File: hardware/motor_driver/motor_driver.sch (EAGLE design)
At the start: 88 parts

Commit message: Shit from Sunday work session
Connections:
- net DC_CAL: now also CURR-4.S; no longer CURR-2.S
- net DGND: now also M-1.S; no longer M-8.S
- net EN_GATE: now also M-2.S; no longer M-1.S
- net H1: now also M-3.S; no longer M-2.S
- net H2: now also M-5.S; no longer M-4.S
- net H3: now also M-7.S; no longer M-6.S
- net L1: now also M-4.S; no longer M-3.S
- net L2: now also M-6.S; no longer M-5.S
- net L3: now also M-8.S; no longer M-7.S
- net REF: now also CURR-3.S; no longer CURR-1.S
- net SO1: now also CURR-2.S; no longer CURR-3.S
- net SO2: now also CURR-1.S; no longer CURR-4.S
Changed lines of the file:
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@@
 <?xml version="1.0" encoding="utf-8"?>
 <!DOCTYPE eagle SYSTEM "eagle.dtd">
-<eagle version="7.3.0">
+<eagle version="7.2.0">
 <drawing>
 <settings>
@@
 </segment>
 <segment>
-<pinref part="M" gate="-2" pin="S"/>
-<wire x1="248.92" y1="45.72" x2="248.92" y2="48.26" width="0.1524" layer="91"/>
-<label x="248.92" y="48.26" size="1.016" layer="95" rot="R90" xref="yes"/>
+<pinref part="M" gate="-3" pin="S"/>
+<wire x1="246.38" y1="45.72" x2="246.38" y2="48.26" width="0.1524" layer="91"/>
+<label x="246.38" y="48.26" size="1.016" layer="95" rot="R90" xref="yes"/>
 </segment>
 </net>
@@
 </segment>
 <segment>
-<pinref part="M" gate="-3" pin="S"/>
-<wire x1="246.38" y1="45.72" x2="246.38" y2="48.26" width="0.1524" layer="91"/>
-<label x="246.38" y="48.26" size="1.016" layer="95" rot="R90" xref="yes"/>
+<pinref part="M" gate="-4" pin="S"/>
+<wire x1="243.84" y1="45.72" x2="243.84" y2="48.26" width="0.1524" layer="91"/>
+<label x="243.84" y="48.26" size="1.016" layer="95" rot="R90" xref="yes"/>
 </segment>
 </net>
@@
 </segment>
 <segment>
-<pinref part="M" gate="-4" pin="S"/>
-<wire x1="243.84" y1="45.72" x2="243.84" y2="48.26" width="0.1524" layer="91"/>
-<label x="243.84" y="48.26" size="1.016" layer="95" rot="R90" xref="yes"/>
+<pinref part="M" gate="-5" pin="S"/>
+<wire x1="241.3" y1="45.72" x2="241.3" y2="48.26" width="0.1524" layer="91"/>
+<label x="241.3" y="48.26" size="1.016" layer="95" rot="R90" xref="yes"/>
 </segment>
 </net>
@@
 </segment>
 <segment>
-<pinref part="M" gate="-5" pin="S"/>
-<wire x1="241.3" y1="45.72" x2="241.3" y2="48.26" width="0.1524" layer="91"/>
-<label x="241.3" y="48.26" size="1.016" layer="95" rot="R90" xref="yes"/>
+<pinref part="M" gate="-6" pin="S"/>
+<wire x1="238.76" y1="45.72" x2="238.76" y2="48.26" width="0.1524" layer="91"/>
+<label x="238.76" y="48.26" size="1.016" layer="95" rot="R90" xref="yes"/>
 </segment>
 </net>
@@
 </segment>
 <segment>
-<pinref part="M" gate="-6" pin="S"/>
-<wire x1="238.76" y1="45.72" x2="238.76" y2="48.26" width="0.1524" layer="91"/>
-<label x="238.76" y="48.26" size="1.016" layer="95" rot="R90" xref="yes"/>
+<pinref part="M" gate="-7" pin="S"/>
+<wire x1="236.22" y1="45.72" x2="236.22" y2="48.26" width="0.1524" layer="91"/>
+<label x="236.22" y="48.26" size="1.016" layer="95" rot="R90" xref="yes"/>
 </segment>
 </net>
@@
 </segment>
 <segment>
-<pinref part="M" gate="-7" pin="S"/>
-<wire x1="236.22" y1="45.72" x2="236.22" y2="48.26" width="0.1524" layer="91"/>
-<label x="236.22" y="48.26" size="1.016" layer="95" rot="R90" xref="yes"/>
+<pinref part="M" gate="-8" pin="S"/>
+<wire x1="233.68" y1="45.72" x2="233.68" y2="48.26" width="0.1524" layer="91"/>
+<label x="233.68" y="48.26" size="1.016" layer="95" rot="R90" xref="yes"/>
 </segment>
 </net>
@@
 </segment>
 <segment>
-<pinref part="M" gate="-1" pin="S"/>
-<wire x1="251.46" y1="45.72" x2="251.46" y2="48.26" width="0.1524" layer="91"/>
-<label x="251.46" y="48.26" size="1.016" layer="95" rot="R90" xref="yes"/>
+<pinref part="M" gate="-2" pin="S"/>
+<wire x1="248.92" y1="45.72" x2="248.92" y2="48.26" width="0.1524" layer="91"/>
+<label x="248.92" y="48.26" size="1.016" layer="95" rot="R90" xref="yes"/>
 </segment>
 </net>
@@
 </segment>
 <segment>
-<pinref part="CURR" gate="-2" pin="S"/>
-<wire x1="259.08" y1="-78.74" x2="259.08" y2="-76.2" width="0.1524" layer="91"/>
-<label x="259.08" y="-78.74" size="1.016" layer="95" rot="R270" xref="yes"/>
+<pinref part="CURR" gate="-4" pin="S"/>
+<wire x1="264.16" y1="-76.2" x2="264.16" y2="-78.74" width="0.1524" layer="91"/>
+<label x="264.16" y="-78.74" size="1.016" layer="95" rot="R270" xref="yes"/>
 </segment>
 </net>
@@
 </segment>
 <segment>
-<pinref part="CURR" gate="-1" pin="S"/>
-<wire x1="256.54" y1="-78.74" x2="256.54" y2="-76.2" width="0.1524" layer="91"/>
-<label x="256.54" y="-78.74" size="1.016" layer="95" rot="R270" xref="yes"/>
+<pinref part="CURR" gate="-3" pin="S"/>
+<wire x1="261.62" y1="-78.74" x2="261.62" y2="-76.2" width="0.1524" layer="91"/>
+<label x="261.62" y="-78.74" size="1.016" layer="95" rot="R270" xref="yes"/>
 </segment>
 </net>
@@
 </segment>
 <segment>
-<pinref part="CURR" gate="-4" pin="S"/>
-<wire x1="264.16" y1="-76.2" x2="264.16" y2="-78.74" width="0.1524" layer="91"/>
-<label x="264.16" y="-78.74" size="1.016" layer="95" rot="R270" xref="yes"/>
+<pinref part="CURR" gate="-1" pin="S"/>
+<wire x1="256.54" y1="-78.74" x2="256.54" y2="-76.2" width="0.1524" layer="91"/>
+<label x="256.54" y="-78.74" size="1.016" layer="95" rot="R270" xref="yes"/>
 </segment>
 </net>
@@
 </segment>
 <segment>
-<pinref part="CURR" gate="-3" pin="S"/>
-<wire x1="261.62" y1="-78.74" x2="261.62" y2="-76.2" width="0.1524" layer="91"/>
-<label x="261.62" y="-78.74" size="1.016" layer="95" rot="R270" xref="yes"/>
+<pinref part="CURR" gate="-2" pin="S"/>
+<wire x1="259.08" y1="-78.74" x2="259.08" y2="-76.2" width="0.1524" layer="91"/>
+<label x="259.08" y="-78.74" size="1.016" layer="95" rot="R270" xref="yes"/>
 </segment>
 </net>
@@
 </segment>
 <segment>
-<pinref part="M" gate="-8" pin="S"/>
-<wire x1="233.68" y1="45.72" x2="233.68" y2="48.26" width="0.1524" layer="91"/>
-<label x="233.68" y="48.26" size="1.016" layer="95" rot="R90" xref="yes"/>
-</segment>
-<segment>
 <pinref part="R16" gate="G$1" pin="1"/>
 <pinref part="SUPPLY6" gate="G$1" pin="DGND"/>
@@
 <pinref part="SUPPLY13" gate="G$1" pin="DGND"/>
 </segment>
-</net>
+<segment>
+<pinref part="M" gate="-1" pin="S"/>
+<wire x1="251.46" y1="45.72" x2="251.46" y2="48.26" width="0.1524" layer="91"/>
+<label x="251.46" y="48.26" size="1.016" layer="95" rot="R90" xref="yes"/>
+</segment>
+</net>

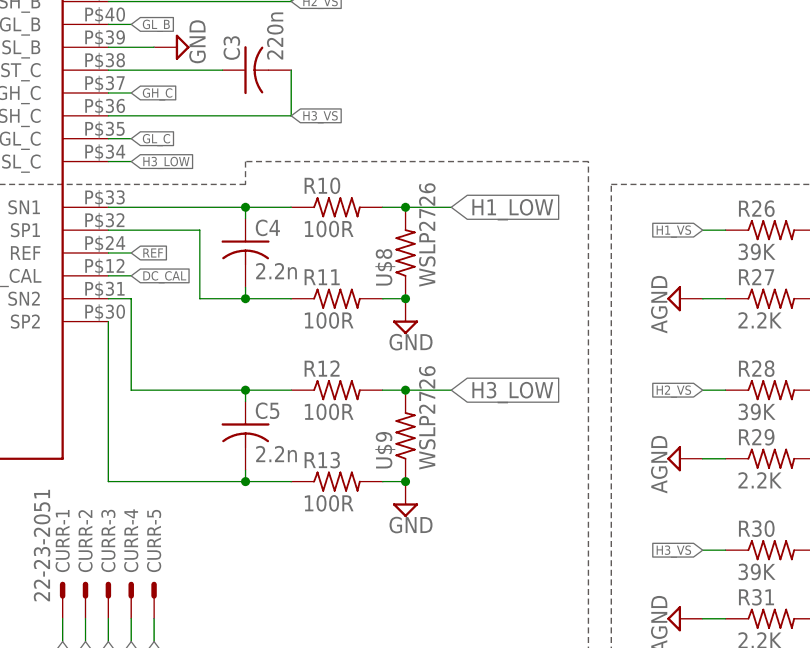
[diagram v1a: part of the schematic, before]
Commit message: Changed shunt resistor sch, needs confirmtion
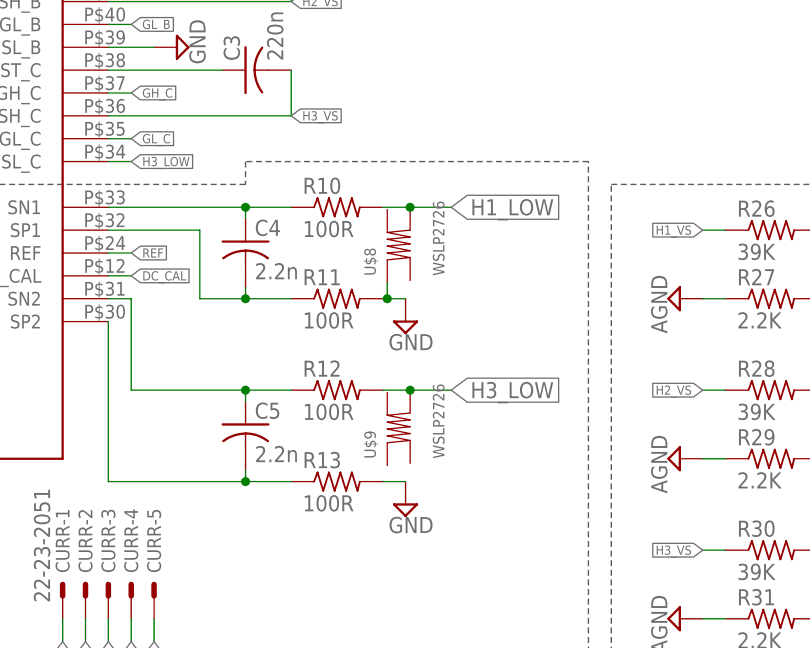
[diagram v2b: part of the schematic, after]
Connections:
- net GND: now also U$8.P$4; no longer U$8.1, U$9.1
- net H1_LOW: now also U$8.P$1; no longer U$8.2
- net H3_LOW: now also U$9.P$1; no longer U$9.2
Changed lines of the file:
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@@
 <part name="R12" library="adafruit" deviceset="R-US_" device="R0603" value="100R"/>
 <part name="R13" library="adafruit" deviceset="R-US_" device="R0603" value="100R"/>
-<part name="U$8" library="bldc_lib" deviceset="WSLP2726" device=""/>
-<part name="U$9" library="bldc_lib" deviceset="WSLP2726" device=""/>
 <part name="SUPPLY1" library="supply2" deviceset="GND" device=""/>
 <part name="SUPPLY2" library="supply2" deviceset="GND" device=""/>
@@
 <part name="SUPPLY27" library="supply2" deviceset="GND" device=""/>
 <part name="SUPPLY13" library="supply2" deviceset="DGND" device=""/>
+<part name="U$8" library="bldc_lib" deviceset="WSLP2726" device=""/>
+<part name="U$9" library="bldc_lib" deviceset="WSLP2726" device=""/>
 </parts>
 <sheets>
@@
 <instance part="R12" gate="G$1" x="287.02" y="-50.8"/>
 <instance part="R13" gate="G$1" x="287.02" y="-60.96"/>
-<instance part="U$8" gate="R$1" x="294.64" y="-35.56" rot="R90"/>
-<instance part="U$9" gate="R$1" x="294.64" y="-55.88" rot="R90"/>
 <instance part="SUPPLY1" gate="GND" x="294.64" y="-43.18"/>
 <instance part="SUPPLY2" gate="GND" x="294.64" y="-63.5"/>
@@
 <instance part="SUPPLY27" gate="GND" x="269.24" y="-12.7" rot="R90"/>
 <instance part="SUPPLY13" gate="G$1" x="200.66" y="-17.78" rot="R180"/>
+<instance part="U$8" gate="G$1" x="293.878" y="-35.56" rot="R90"/>
+<instance part="U$9" gate="G$1" x="293.878" y="-55.88" rot="R90"/>
 </instances>
 <busses>
@@
 <segment>
 <pinref part="R10" gate="G$1" pin="2"/>
-<pinref part="U$8" gate="R$1" pin="2"/>
-<wire x1="292.1" y1="-30.48" x2="294.64" y2="-30.48" width="0.1524" layer="91"/>
-<wire x1="294.64" y1="-30.48" x2="299.72" y2="-30.48" width="0.1524" layer="91"/>
-<junction x="294.64" y="-30.48"/>
+<wire x1="292.1" y1="-30.48" x2="295.148" y2="-30.48" width="0.1524" layer="91"/>
 <label x="299.72" y="-30.48" size="1.778" layer="95" xref="yes"/>
+<pinref part="U$8" gate="G$1" pin="P$1"/>
+<wire x1="295.148" y1="-30.48" x2="299.72" y2="-30.48" width="0.1524" layer="91"/>
+<junction x="295.148" y="-30.48"/>
 </segment>
 </net>
@@
 </segment>
 <segment>
-<pinref part="U$9" gate="R$1" pin="2"/>
 <pinref part="R12" gate="G$1" pin="2"/>
-<wire x1="294.64" y1="-50.8" x2="292.1" y2="-50.8" width="0.1524" layer="91"/>
-<wire x1="294.64" y1="-50.8" x2="299.72" y2="-50.8" width="0.1524" layer="91"/>
-<junction x="294.64" y="-50.8"/>
+<wire x1="292.1" y1="-50.8" x2="295.148" y2="-50.8" width="0.1524" layer="91"/>
 <label x="299.72" y="-50.8" size="1.778" layer="95" xref="yes"/>
+<pinref part="U$9" gate="G$1" pin="P$1"/>
+<wire x1="295.148" y1="-50.8" x2="299.72" y2="-50.8" width="0.1524" layer="91"/>
+<junction x="295.148" y="-50.8"/>
 </segment>
 </net>
@@
 <segment>
 <pinref part="R11" gate="G$1" pin="2"/>
-<pinref part="U$8" gate="R$1" pin="1"/>
-<wire x1="292.1" y1="-40.64" x2="294.64" y2="-40.64" width="0.1524" layer="91"/>
+<wire x1="292.1" y1="-40.64" x2="292.608" y2="-40.64" width="0.1524" layer="91"/>
 <pinref part="SUPPLY1" gate="GND" pin="GND"/>
-<junction x="294.64" y="-40.64"/>
-</segment>
-<segment>
-<pinref part="U$9" gate="R$1" pin="1"/>
+<pinref part="U$8" gate="G$1" pin="P$4"/>
+<wire x1="292.608" y1="-40.64" x2="294.64" y2="-40.64" width="0.1524" layer="91"/>
+<wire x1="292.608" y1="-38.862" x2="292.608" y2="-40.64" width="0.1524" layer="91"/>
+<junction x="292.608" y="-40.64"/>
+</segment>
+<segment>
 <pinref part="R13" gate="G$1" pin="2"/>
 <wire x1="294.64" y1="-60.96" x2="292.1" y2="-60.96" width="0.1524" layer="91"/>
 <pinref part="SUPPLY2" gate="GND" pin="GND"/>
-<junction x="294.64" y="-60.96"/>
-</segment>
-<segment>
+</segment>
+<segment>

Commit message: Almost there
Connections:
- new net N$124: R12.2, U$9.P$3
- new net N$126: R10.2, U$8.P$3
- new net N$127: R11.2, U$8.P$4
- new net N$128: R13.2, U$9.P$4
- net GND: now also U$8.P$2, U$9.P$2; no longer R11.2, R13.2, U$8.P$4
- net H1_LOW: no longer R10.2
- net H3_LOW: no longer R12.2
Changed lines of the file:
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@@
 <part name="R12" library="adafruit" deviceset="R-US_" device="R0603" value="100R"/>
 <part name="R13" library="adafruit" deviceset="R-US_" device="R0603" value="100R"/>
-<part name="SUPPLY1" library="supply2" deviceset="GND" device=""/>
 <part name="SUPPLY2" library="supply2" deviceset="GND" device=""/>
 <part name="CURR" library="con-molex" deviceset="22-23-2051" device=""/>
@@
 <part name="U$8" library="bldc_lib" deviceset="WSLP2726" device=""/>
 <part name="U$9" library="bldc_lib" deviceset="WSLP2726" device=""/>
+<part name="SUPPLY28" library="supply2" deviceset="GND" device=""/>
 </parts>
 <sheets>
@@
 <instance part="R12" gate="G$1" x="287.02" y="-50.8"/>
 <instance part="R13" gate="G$1" x="287.02" y="-60.96"/>
-<instance part="SUPPLY1" gate="GND" x="294.64" y="-43.18"/>
-<instance part="SUPPLY2" gate="GND" x="294.64" y="-63.5"/>
+<instance part="SUPPLY2" gate="GND" x="295.148" y="-63.5"/>
 <instance part="CURR" gate="-1" x="256.54" y="-73.66" rot="R90"/>
 <instance part="CURR" gate="-2" x="259.08" y="-73.66" rot="R90"/>
@@
 <instance part="U$8" gate="G$1" x="293.878" y="-35.56" rot="R90"/>
 <instance part="U$9" gate="G$1" x="293.878" y="-55.88" rot="R90"/>
+<instance part="SUPPLY28" gate="GND" x="295.148" y="-41.91"/>
 </instances>
 <busses>
@@
 </segment>
 <segment>
-<pinref part="R10" gate="G$1" pin="2"/>
-<wire x1="292.1" y1="-30.48" x2="295.148" y2="-30.48" width="0.1524" layer="91"/>
-<label x="299.72" y="-30.48" size="1.778" layer="95" xref="yes"/>
 <pinref part="U$8" gate="G$1" pin="P$1"/>
 <wire x1="295.148" y1="-30.48" x2="299.72" y2="-30.48" width="0.1524" layer="91"/>
-<junction x="295.148" y="-30.48"/>
+<label x="299.72" y="-30.48" size="1.778" layer="95" xref="yes"/>
 </segment>
 </net>
@@
 </segment>
 <segment>
-<pinref part="R12" gate="G$1" pin="2"/>
-<wire x1="292.1" y1="-50.8" x2="295.148" y2="-50.8" width="0.1524" layer="91"/>
 <label x="299.72" y="-50.8" size="1.778" layer="95" xref="yes"/>
 <pinref part="U$9" gate="G$1" pin="P$1"/>
 <wire x1="295.148" y1="-50.8" x2="299.72" y2="-50.8" width="0.1524" layer="91"/>
-<junction x="295.148" y="-50.8"/>
 </segment>
 </net>
@@
 </net>
 <net name="GND" class="0">
-<segment>
-<pinref part="R11" gate="G$1" pin="2"/>
-<wire x1="292.1" y1="-40.64" x2="292.608" y2="-40.64" width="0.1524" layer="91"/>
-<pinref part="SUPPLY1" gate="GND" pin="GND"/>
-<pinref part="U$8" gate="G$1" pin="P$4"/>
-<wire x1="292.608" y1="-40.64" x2="294.64" y2="-40.64" width="0.1524" layer="91"/>
-<wire x1="292.608" y1="-38.862" x2="292.608" y2="-40.64" width="0.1524" layer="91"/>
-<junction x="292.608" y="-40.64"/>
-</segment>
-<segment>
-<pinref part="R13" gate="G$1" pin="2"/>
-<wire x1="294.64" y1="-60.96" x2="292.1" y2="-60.96" width="0.1524" layer="91"/>
-<pinref part="SUPPLY2" gate="GND" pin="GND"/>
-</segment>
 <segment>
 <pinref part="C12" gate="G$1" pin="2"/>
@@
 <wire x1="261.62" y1="-12.7" x2="266.7" y2="-12.7" width="0.1524" layer="91"/>
 <pinref part="SUPPLY27" gate="GND" pin="GND"/>
+</segment>
+<segment>
+<pinref part="U$8" gate="G$1" pin="P$2"/>
+<wire x1="295.148" y1="-38.608" x2="295.148" y2="-39.37" width="0.1524" layer="91"/>
+<pinref part="SUPPLY28" gate="GND" pin="GND"/>
+</segment>
+<segment>
+<pinref part="U$9" gate="G$1" pin="P$2"/>
+<pinref part="SUPPLY2" gate="GND" pin="GND"/>
+<wire x1="295.148" y1="-58.928" x2="295.148" y2="-60.96" width="0.1524" layer="91"/>
 </segment>
 </net>
@@
 </segment>
 </net>
+<net name="N$126" class="0">
+<segment>
+<pinref part="R10" gate="G$1" pin="2"/>
+<pinref part="U$8" gate="G$1" pin="P$3"/>
+<wire x1="292.1" y1="-30.48" x2="292.608" y2="-30.48" width="0.1524" layer="91"/>
+<wire x1="292.608" y1="-30.48" x2="292.608" y2="-30.734" width="0.1524" layer="91"/>
+</segment>
+</net>
+<net name="N$127" class="0">
+<segment>
+<pinref part="U$8" gate="G$1" pin="P$4"/>
+<wire x1="292.608" y1="-38.862" x2="292.608" y2="-40.64" width="0.1524" layer="91"/>
+<pinref part="R11" gate="G$1" pin="2"/>
+<wire x1="292.608" y1="-40.64" x2="292.1" y2="-40.64" width="0.1524" layer="91"/>
+</segment>
+</net>
+<net name="N$128" class="0">
+<segment>
+<pinref part="R13" gate="G$1" pin="2"/>
+<pinref part="U$9" gate="G$1" pin="P$4"/>
+<wire x1="292.608" y1="-60.96" x2="292.1" y2="-60.96" width="0.1524" layer="91"/>
+<wire x1="292.608" y1="-59.182" x2="292.608" y2="-60.96" width="0.1524" layer="91"/>
+</segment>
+</net>
+<net name="N$124" class="0">
+<segment>
+<pinref part="R12" gate="G$1" pin="2"/>
+<pinref part="U$9" gate="G$1" pin="P$3"/>
+<wire x1="292.1" y1="-50.8" x2="292.608" y2="-50.8" width="0.1524" layer="91"/>
+<wire x1="292.608" y1="-50.8" x2="292.608" y2="-51.054" width="0.1524" layer="91"/>
+</segment>
+</net>
